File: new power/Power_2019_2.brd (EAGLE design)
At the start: 103 x 74.5 mm, 58 parts, among them IC1 ATMEGA328P_PDIP, IC2 LT1161, IC4 LT1161, Q5 16MHz, Q8 16MHz, U1 MCP2515, X1 MABC96R

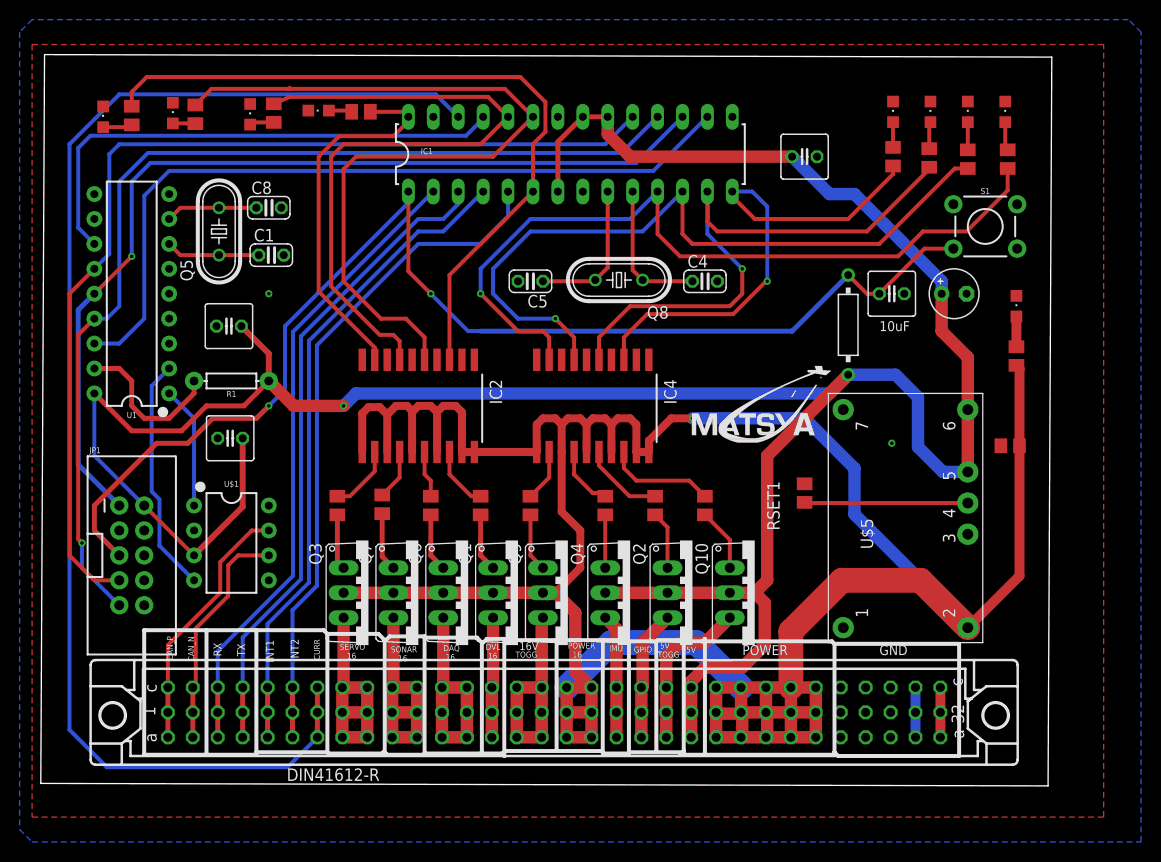
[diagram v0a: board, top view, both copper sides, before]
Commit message: power labelling done
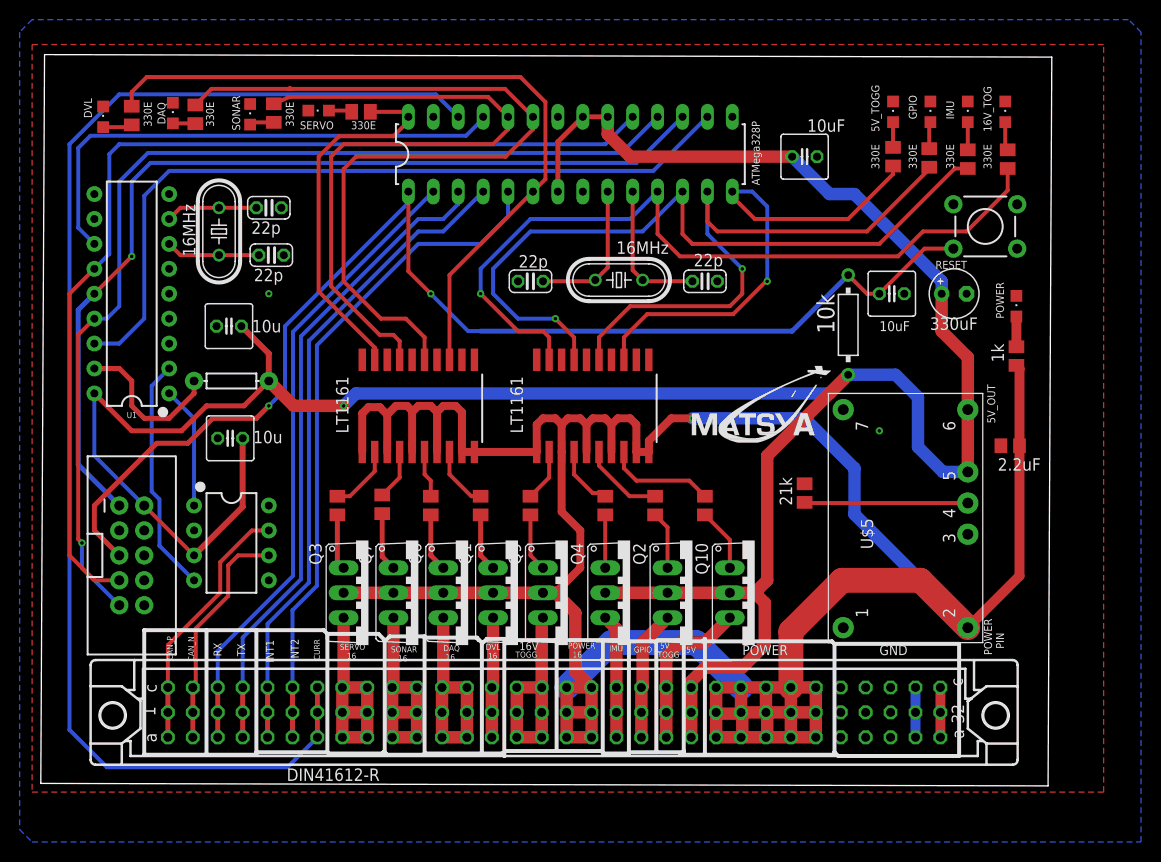
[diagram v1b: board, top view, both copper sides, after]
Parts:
- C9: value 10uF -> 10u
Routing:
- net A_DAQ: track 82.2 -> 82.9 mm
- net A_SONAR: track 69.0 -> 69.7 mm
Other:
- board text added: "16V_TOG"
- board text added: "330E"
- board text added: "5V_OUT"
- board text added: "5V_TOGG"
- board text added: "ATMega328P"
- board text added: "DAQ"
- board text added: "DVL"
- board text added: "POWER PIN"
- board text added: "RESET"
- board text added: "SERVO"
- board text added: "SONAR"
